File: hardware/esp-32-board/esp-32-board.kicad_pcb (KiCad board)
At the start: 2 copper layers, 53.8 x 69.1 mm, 34 parts, among them J1 MainConnector, J2 Conn_01x06, J3 ESP-PROG-Program, J4 ESP-PROG-Debug, J5 USB_B_Micro, J6 Barrel_Jack_MountingPin, Q1 BCR129S, SW1 SW_Push, SW2 SW_Push, SW3 SW_DPDT_x2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

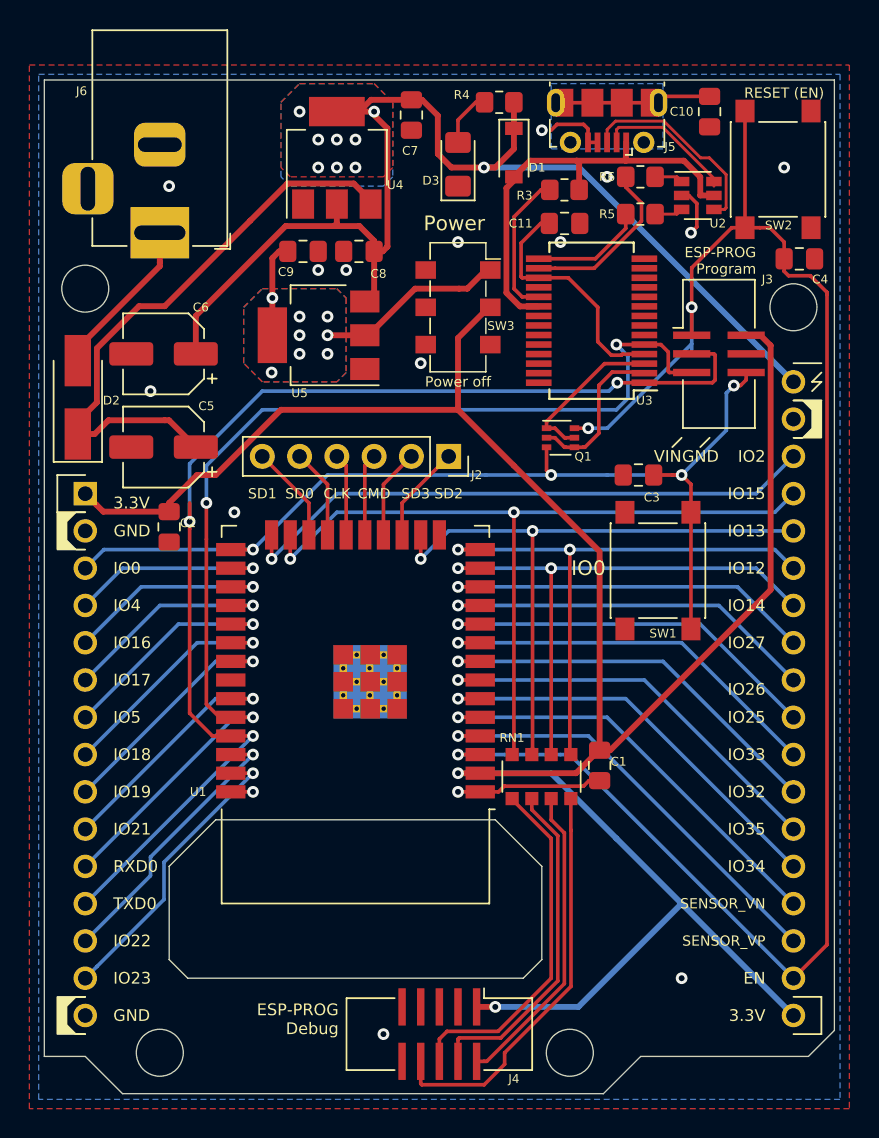
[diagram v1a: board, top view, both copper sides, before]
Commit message: Change shape of antenna cutoff and tracks around it
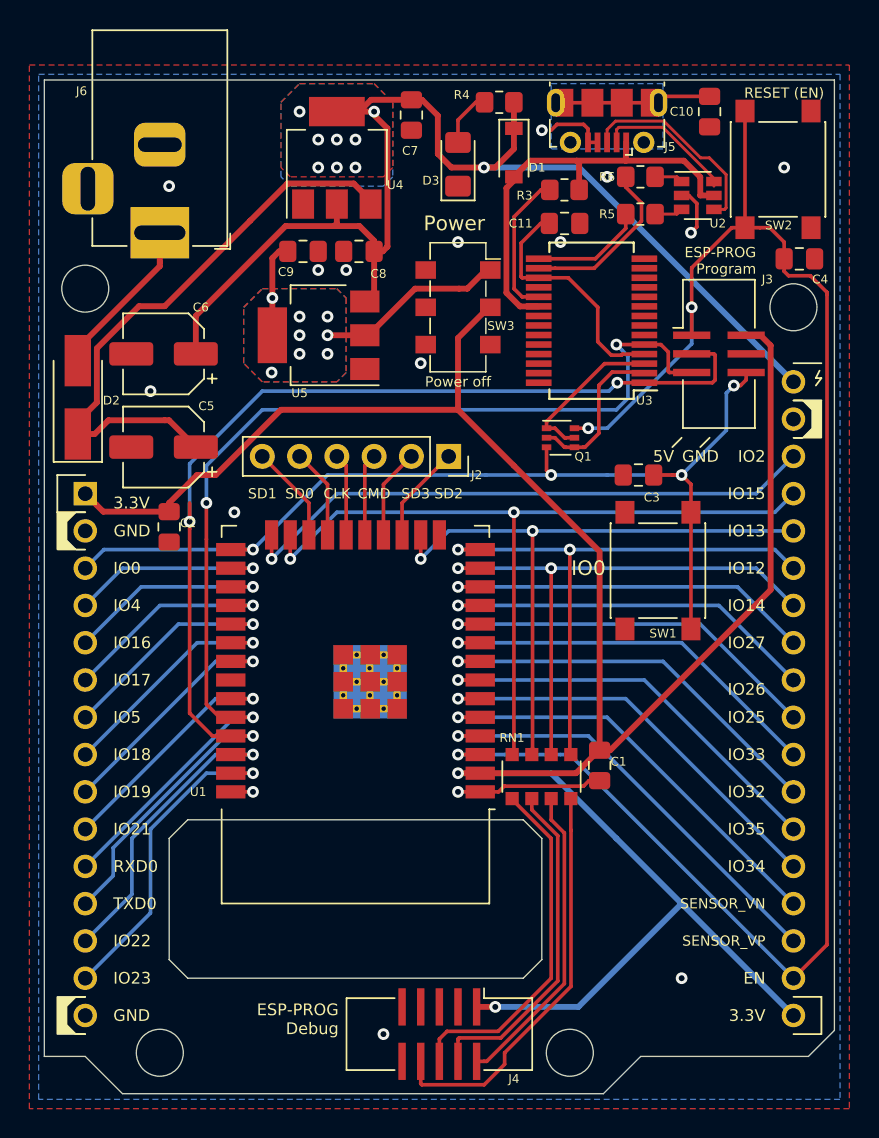
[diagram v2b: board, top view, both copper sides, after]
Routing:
- net /IO23: track 20.2 -> 22.1 mm
- net /IO22: track 18.9 -> 20.4 mm
- net /TXD0: track 80.9 -> 82.0 mm
- net /EN: track 117.8 -> 117.1 mm
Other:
- outline, holes or cut-outs redrawn
- board text added: "5V"
- board text removed: "VIN"
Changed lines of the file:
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@@
     (thickness 1.6)
     (drawings 78)
-    (tracks 538)
+    (tracks 546)
     (zones 0)
     (modules 34)
@@
     (34 B.Paste user hide)
     (35 F.Paste user hide)
-    (36 B.SilkS user hide)
+    (36 B.SilkS user)
     (37 F.SilkS user)
     (38 B.Mask user hide)
@@
     (add_net "Net-(C11-Pad1)")
     (add_net "Net-(D3-Pad2)")
+    (add_net "Net-(J4-Pad10)")
     (add_net "Net-(J4-Pad2)")
     (add_net "Net-(J4-Pad4)")
@@
     (add_net "Net-(R5-Pad1)")
     (add_net "Net-(R6-Pad1)")
+    (add_net "Net-(SW3-Pad3)")
+    (add_net "Net-(U1-Pad32)")
+    (add_net "Net-(U3-Pad10)")
+    (add_net "Net-(U3-Pad11)")
+    (add_net "Net-(U3-Pad12)")
+    (add_net "Net-(U3-Pad13)")
+    (add_net "Net-(U3-Pad14)")
+    (add_net "Net-(U3-Pad22)")
+    (add_net "Net-(U3-Pad23)")
+    (add_net "Net-(U3-Pad27)")
+    (add_net "Net-(U3-Pad28)")
+    (add_net "Net-(U3-Pad6)")
+    (add_net "Net-(U3-Pad9)")
   )
   (net_class Power ""
@@
   (module project_components:MainConnector locked (layer B.Cu)
     (at 132.08 49.53 270)
-    (fp_text reference J1 (at 1.27 3.81 270) (layer B.SilkS)
+    (fp_text reference J1 (at 1.27 3.81 270) (layer B.SilkS) hide
       (effects (font (size 1 1) (thickness 0.15)) (justify mirror))
     )
-    (fp_text value MainConnector (at 0 -22.86 90) (layer B.Fab)
+    (fp_text value MainConnector (at 0 -22.86 90) (layer B.Fab) hide
       (effects (font (size 1 1) (thickness 0.15)) (justify mirror))
     )
@@
     (fp_line (start 38.35 0) (end 40.89 -2.54) (layer B.CrtYd) (width 0.05))
     (fp_line (start 38.35 2.79) (end 38.35 0) (layer B.CrtYd) (width 0.05))
-    (fp_text user %R (at 0 -20.32 270) (layer B.Fab)
+    (fp_text user %R (at 0 -20.32 270) (layer B.Fab) hide
       (effects (font (size 1 1) (thickness 0.15)) (justify mirror))
     )
@@
     (pad 32 thru_hole oval (at -5.08 -48.26 180) (size 1.6 1.6) (drill 1) (layers *.Cu *.Mask)
       (net 1 GND))
+    (model ${KIPRJMOD}/project_packages3d/MainConnector.wrl
+      (at (xyz 0 0 0))
+      (scale (xyz 1 1 1))
+      (rotate (xyz 0 0 0))
+    )
   )
   (module Capacitor_SMD:C_0805_2012Metric_Pad1.18x1.45mm_HandSolder (layer F.Cu)
@@
     )
   )
-  (gr_line (start 182.245 41.91) (end 181.61 42.545) (layer F.SilkS) (width 0.12))
-  (gr_line (start 181.61 41.91) (end 182.245 41.91) (layer F.SilkS) (width 0.12))
-  (gr_line (start 182.245 41.275) (end 181.61 41.91) (layer F.SilkS) (width 0.12))
+  (gr_line (start 182.245 41.656) (end 181.864 42.164) (layer F.SilkS) (width 0.12))
+  (gr_line (start 181.864 41.656) (end 182.245 41.656) (layer F.SilkS) (width 0.12))
+  (gr_line (start 182.118 41.148) (end 181.864 41.656) (layer F.SilkS) (width 0.12))
   (gr_line (start 130.175 48.26) (end 132.08 48.26) (layer F.SilkS) (width 0.12))
   (gr_line (start 132.08 50.8) (end 130.175 50.8) (layer F.SilkS) (width 0.12))
@@
   (gr_line (start 161.925 82.55) (end 163.195 81.28) (layer Edge.Cuts) (width 0.05))
   (gr_line (start 137.795 81.28) (end 139.065 82.55) (layer Edge.Cuts) (width 0.05))
-  (gr_line (start 160.02 71.755) (end 140.97 71.755) (layer Edge.Cuts) (width 0.05))
-  (gr_line (start 163.195 74.93) (end 160.02 71.755) (layer Edge.Cuts) (width 0.05))
-  (gr_line (start 163.195 81.28) (end 163.195 74.93) (layer Edge.Cuts) (width 0.05))
+  (gr_line (start 161.925 71.755) (end 139.065 71.755) (layer Edge.Cuts) (width 0.05))
+  (gr_line (start 163.195 73.025) (end 161.925 71.755) (layer Edge.Cuts) (width 0.05))
+  (gr_line (start 163.195 81.28) (end 163.195 73.025) (layer Edge.Cuts) (width 0.05))
   (gr_line (start 139.065 82.55) (end 161.925 82.55) (layer Edge.Cuts) (width 0.05))
-  (gr_line (start 137.795 74.93) (end 137.795 81.28) (layer Edge.Cuts) (width 0.05))
-  (gr_line (start 140.97 71.755) (end 137.795 74.93) (layer Edge.Cuts) (width 0.05))
+  (gr_line (start 137.795 73.025) (end 137.795 81.28) (layer Edge.Cuts) (width 0.05))
+  (gr_line (start 139.065 71.755) (end 137.795 73.025) (layer Edge.Cuts) (width 0.05))
   (gr_text "Power off" (at 157.48 41.91) (layer F.SilkS)
     (effects (font (size 0.7 0.7) (thickness 0.175)))
@@
     (effects (font (size 0.8 0.8) (thickness 0.15)) (justify left))
   )
-  (gr_text VIN (at 172.72 46.99) (layer F.SilkS)
+  (gr_text 5V (at 172.212 46.99) (layer F.SilkS)
     (effects (font (size 0.8 0.8) (thickness 0.15)) (justify right))
   )
@@
   (segment (start 168.275 43.815) (end 169.060001 43.029999) (width 0.25) (layer B.Cu) (net 33))
   (segment (start 143.51 64.77) (end 143.51 64.77) (width 0.25) (layer F.Cu) (net 33))
-  (via (at 143.51 64.77) (size 0.8) (drill 0.4) (layers F.Cu B.Cu) (net 33))
-  (segment (start 142.24 64.77) (end 132.08 74.93) (width 0.25) (layer B.Cu) (net 33))
-  (segment (start 143.51 64.77) (end 142.24 64.77) (width 0.25) (layer B.Cu) (net 33))
   (segment (start 141.995 66.04) (end 143.51 66.04) (width 0.25) (layer F.Cu) (net 34))
   (segment (start 143.51 66.04) (end 143.51 66.04) (width 0.25) (layer F.Cu) (net 34))
@@
   (segment (start 167.76 42.545) (end 144.145 42.545) (width 0.25) (layer B.Cu) (net 34))
   (segment (start 143.51 66.04) (end 143.51 66.04) (width 0.25) (layer F.Cu) (net 34))
-  (via (at 143.51 66.04) (size 0.8) (drill 0.4) (layers F.Cu B.Cu) (net 34))
-  (segment (start 143.51 66.04) (end 132.08 77.47) (width 0.25) (layer B.Cu) (net 34))
   (segment (start 141.995 67.31) (end 143.51 67.31) (width 0.25) (layer F.Cu) (net 35))
   (segment (start 143.51 67.31) (end 143.51 67.31) (width 0.25) (layer F.Cu) (net 35))
@@
   (segment (start 143.51 67.31) (end 143.51 67.31) (width 0.25) (layer F.Cu) (net 35))
   (segment (start 143.51 67.31) (end 143.51 67.31) (width 0.25) (layer F.Cu) (net 35))
-  (via (at 143.51 67.31) (size 0.8) (drill 0.4) (layers F.Cu B.Cu) (net 35))
-  (segment (start 143.51 67.31) (end 136.525 74.295) (width 0.25) (layer B.Cu) (net 35))
-  (segment (start 136.525 75.565) (end 132.08 80.01) (width 0.25) (layer B.Cu) (net 35))
-  (segment (start 136.525 74.295) (end 136.525 75.565) (width 0.25) (layer B.Cu) (net 35))
   (segment (start 141.995 68.58) (end 143.51 68.58) (width 0.25) (layer F.Cu) (net 36))
   (segment (start 143.51 68.58) (end 143.51 68.58) (width 0.25) (layer F.Cu) (net 36))
@@
   (segment (start 143.51 68.58) (end 143.51 68.58) (width 0.25) (layer F.Cu) (net 36))
   (segment (start 143.51 68.58) (end 143.51 68.58) (width 0.25) (layer F.Cu) (net 36))
-  (via (at 143.51 68.58) (size 0.8) (drill 0.4) (layers F.Cu B.Cu) (net 36))
-  (segment (start 132.879999 81.750001) (end 132.08 82.55) (width 0.25) (layer B.Cu) (net 36))
-  (segment (start 137.44499 77.18501) (end 132.879999 81.750001) (width 0.25) (layer B.Cu) (net 36))
-  (segment (start 137.44499 74.64501) (end 137.44499 77.18501) (width 0.25) (layer B.Cu) (net 36))
-  (segment (start 143.51 68.58) (end 137.44499 74.64501) (width 0.25) (layer B.Cu) (net 36))
   (segment (start 168.91 30.48) (end 168.91 31.456782) (width 0.25) (layer F.Cu) (net 37))
   (segment (start 166.846782 33.52) (end 162.98 33.52) (width 0.25) (layer F.Cu) (net 37))
@@
   (segment (start 173.405 34.14) (end 176.138 31.407) (width 0.25) (layer F.Cu) (net 5))
   (segment (start 173.405 38.735) (end 173.405 34.14) (width 0.25) (layer F.Cu) (net 5))
-  (segment (start 173.405 39.95641) (end 173.405 36.83) (width 0.25) (layer B.Cu) (net 5))
   (segment (start 166.355 45.07) (end 167.65641 45.07) (width 0.25) (layer B.Cu) (net 5))
   (segment (start 167.65641 45.07) (end 173.405 39.32141) (width 0.25) (layer B.Cu) (net 5))
+  (segment (start 173.405 36.83) (end 173.405 39.32141) (width 0.25) (layer B.Cu) (net 5))
+  (segment (start 143.51 64.77) (end 143.51 64.77) (width 0.25) (layer F.Cu) (net 33))
+  (via (at 143.51 64.77) (size 0.8) (drill 0.4) (layers F.Cu B.Cu) (net 33))
+  (segment (start 142.24 64.77) (end 132.08 74.93) (width 0.25) (layer B.Cu) (net 33))
+  (segment (start 143.51 64.77) (end 142.24 64.77) (width 0.25) (layer B.Cu) (net 33))
+  (segment (start 143.51 66.04) (end 143.51 66.04) (width 0.25) (layer F.Cu) (net 34))
+  (via (at 143.51 66.04) (size 0.8) (drill 0.4) (layers F.Cu B.Cu) (net 34))
+  (segment (start 143.51 66.04) (end 141.60641 66.04) (width 0.25) (layer B.Cu) (net 34))
+  (segment (start 141.60641 66.04) (end 133.985705 73.660705) (width 0.25) (layer B.Cu) (net 34))
+  (segment (start 133.985705 75.564295) (end 132.08 77.47) (width 0.25) (layer B.Cu) (net 34))
+  (segment (start 133.985705 73.660705) (end 133.985705 75.564295) (width 0.25) (layer B.Cu) (net 34))
+  (segment (start 143.51 67.31) (end 143.51 67.31) (width 0.25) (layer F.Cu) (net 35))
+  (via (at 143.51 67.31) (size 0.8) (drill 0.4) (layers F.Cu B.Cu) (net 35))
+  (segment (start 143.51 67.31) (end 140.97282 67.31) (width 0.25) (layer B.Cu) (net 35))
+  (segment (start 140.97282 67.31) (end 135.25641 73.02641) (width 0.25) (layer B.Cu) (net 35))
+  (segment (start 135.25641 76.83359) (end 132.08 80.01) (width 0.25) (layer B.Cu) (net 35))
+  (segment (start 135.25641 73.02641) (end 135.25641 76.83359) (width 0.25) (layer B.Cu) (net 35))
+  (segment (start 143.51 68.58) (end 143.51 68.58) (width 0.25) (layer F.Cu) (net 36))
+  (via (at 143.51 68.58) (size 0.8) (drill 0.4) (layers F.Cu B.Cu) (net 36))
+  (segment (start 143.51 68.58) (end 140.33923 68.58) (width 0.25) (layer B.Cu) (net 36))
+  (segment (start 140.33923 68.58) (end 136.525 72.39423) (width 0.25) (layer B.Cu) (net 36))
+  (segment (start 136.525 78.105) (end 132.08 82.55) (width 0.25) (layer B.Cu) (net 36))
+  (segment (start 136.525 72.39423) (end 136.525 78.105) (width 0.25) (layer B.Cu) (net 36))
   (via (at 144.83 36.195) (size 0.8) (drill 0.4) (layers F.Cu B.Cu) (net 42))
   (via (at 144.78 41.275) (size 0.8) (drill 0.4) (layers F.Cu B.Cu) (net 42))
@@
       (pts
         (xy 163.83 73.025) (xy 163.83 81.28) (xy 161.925 83.185) (xy 139.065 83.185) (xy 137.16 81.28)
-        (xy 137.16 74.93) (xy 140.97 71.12) (xy 161.925 71.12)
+        (xy 137.16 73.025) (xy 139.065 71.12) (xy 161.925 71.12)
       )
     )

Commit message: Replace 15-pin header with 14-pin one
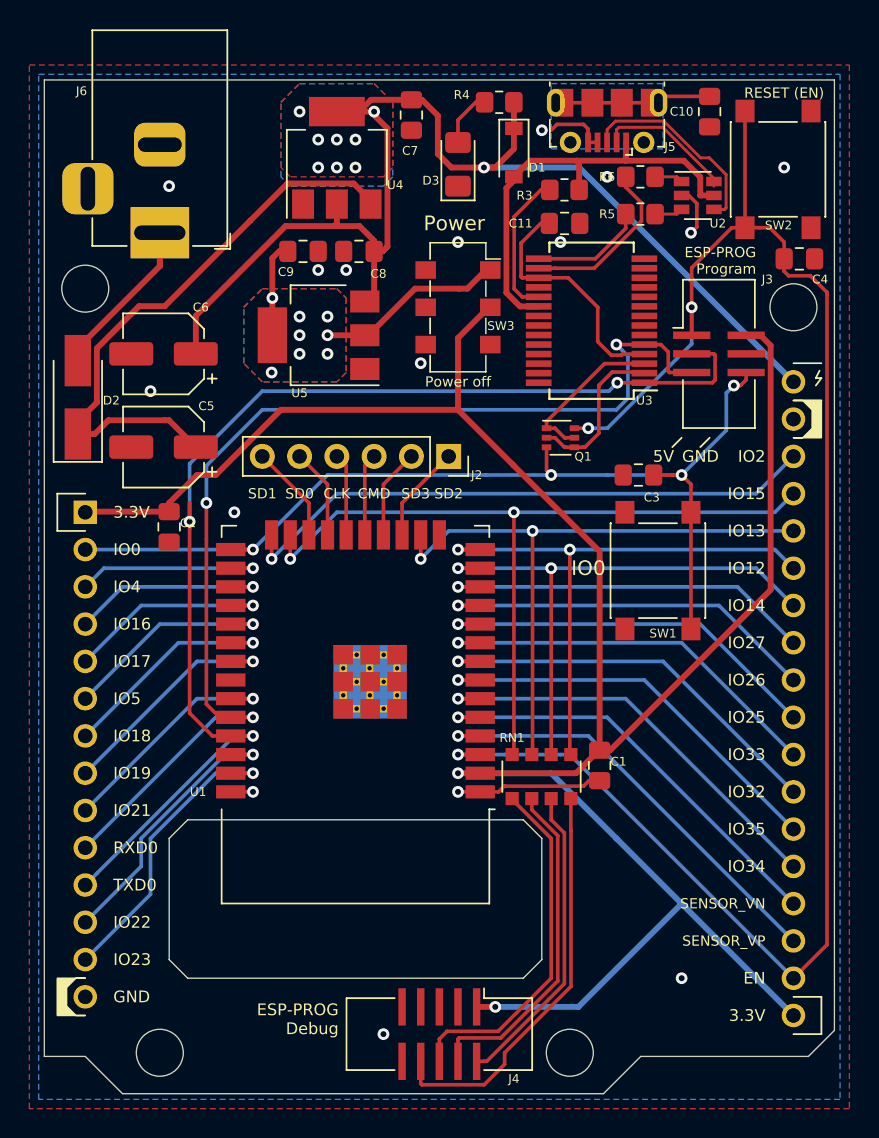
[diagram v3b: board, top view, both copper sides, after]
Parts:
- J1: value MainConnector -> Arduino_UNO_R3_WithMountingHoles
- moved J1 1.27 mm to (132.1, 50.8)
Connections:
- J1 pad 10: /IO21 -> /RXD0
- J1 pad 11: /RXD0 -> /TXD0
- J1 pad 12: /TXD0 -> /IO22
- J1 pad 13: /IO22 -> /IO23
- J1 pad 14: /IO23 -> GND
- J1 pad 15: GND -> +3V3
- J1 pad 16: +3V3 -> /EN
- J1 pad 17: /EN -> /SENSOR_VP
- J1 pad 18: /SENSOR_VP -> /SENSOR_VN
- J1 pad 19: /SENSOR_VN -> /IO34
- J1 pad 2: GND -> /IO0
- J1 pad 20: /IO34 -> /IO35
- J1 pad 21: /IO35 -> /IO32
- J1 pad 22: /IO32 -> /IO33
- J1 pad 23: /IO33 -> /IO25
- J1 pad 24: /IO25 -> /IO26
- J1 pad 25: /IO26 -> /IO27
- J1 pad 26: /IO27 -> /IO14
- J1 pad 27: /IO14 -> /IO12
- J1 pad 28: /IO12 -> /IO13
- J1 pad 29: /IO13 -> /IO15
- J1 pad 3: /IO0 -> /IO4
- J1 pad 30: /IO15 -> /IO2
- J1 pad 31: /IO2 -> GND
- J1 pad 32: GND -> +5V
- J1 pad 4: /IO4 -> /IO16
- J1 pad 5: /IO16 -> /IO17
- J1 pad 6: /IO17 -> /IO5
- J1 pad 7: /IO5 -> /IO18
- J1 pad 8: /IO18 -> /IO19
- J1 pad 9: /IO19 -> /IO21
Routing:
- net /IO22: track 20.4 -> 18.8 mm
- net /IO23: track 22.1 -> 20.4 mm
- net /TXD0: track 82.0 -> 80.4 mm
- net /RXD0: track 76.7 -> 76.2 mm
- net /IO18: track 16.3 -> 15.8 mm
- net /IO16: track 14.5 -> 14.0 mm
- net /IO0: track 68.5 -> 68.0 mm
- net /IO4: track 14.0 -> 13.5 mm
- net /IO5: track 15.6 -> 15.0 mm
- net /IO17: track 15.0 -> 14.5 mm
- net /IO21: track 16.6 -> 16.1 mm
- net /IO19: track 16.6 -> 16.1 mm

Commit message: Update main connector footprint (reverse, remove silkscreen and mark important parts).
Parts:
- J1: value Arduino_UNO_R3_WithMountingHoles -> MainConnector; moved to F.Cu
- turned J1 to 90 degrees
